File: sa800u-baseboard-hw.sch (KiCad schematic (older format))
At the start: 0 parts

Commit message: removed finished remarks
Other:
- note removed: "GENERAL REMARKS:\n-Nice sheet separation\n-Nice and clear signal labeling\n-Use "kmake get-ignore" inside the repo to make git ignore backup\n files\n-Make folder structure flat - move files ../ \n-Make all the sheets A3 format\n-Avoid "space" in file names use "_" instead"
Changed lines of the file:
@@
 F1 "Level_shift_HDMI.sch" 50
 $EndSheet
-Text Notes 625  6150 0    50   ~ 0
-GENERAL REMARKS:\n-Nice sheet separation\n-Nice and clear signal labeling\n-Use "kmake get-ignore" inside the repo to make git ignore backup\n files\n-Make folder structure flat - move files ../ \n-Make all the sheets A3 format\n-Avoid "space" in file names use "_" instead
 $Sheet
 S 600  7000 500  500

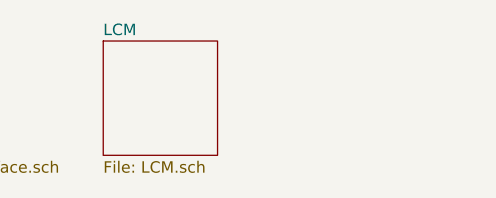
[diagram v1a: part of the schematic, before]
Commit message: finished level shifting circuits for HDMI
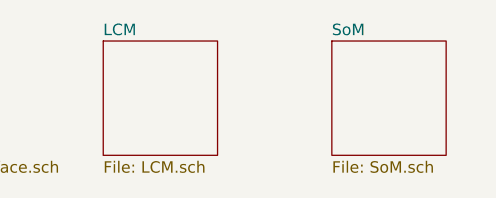
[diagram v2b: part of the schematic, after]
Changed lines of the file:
@@
 $Descr A3 16535 11693
 encoding utf-8
-Sheet 1 7
+Sheet 1 8
 Title ""
 Date ""
@@
 F1 "PoE.sch" 50
 $EndSheet
+$Sheet
+S 7250 7000 500  500
+U 61A4BC4F
+F0 "SoM" 50
+F1 "SoM.sch" 50
+$EndSheet
 $EndSCHEMATC

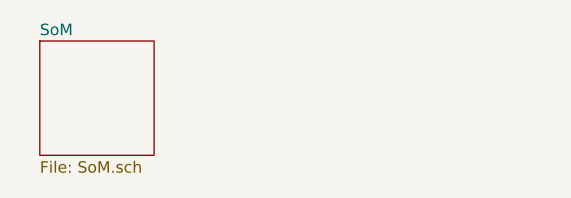
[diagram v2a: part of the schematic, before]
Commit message: added Cameras interface and finished SoM model and symbol
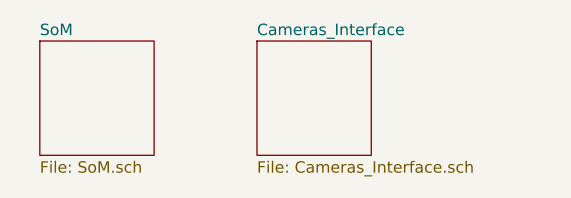
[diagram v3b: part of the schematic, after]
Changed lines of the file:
@@
 $Descr A3 16535 11693
 encoding utf-8
-Sheet 1 8
+Sheet 1 9
 Title ""
 Date ""
@@
 F1 "SoM.sch" 50
 $EndSheet
+$Sheet
+S 8200 7000 500  500
+U 61A60486
+F0 "Cameras_Interface" 50
+F1 "Cameras_Interface.sch" 50
+$EndSheet
 $EndSCHEMATC

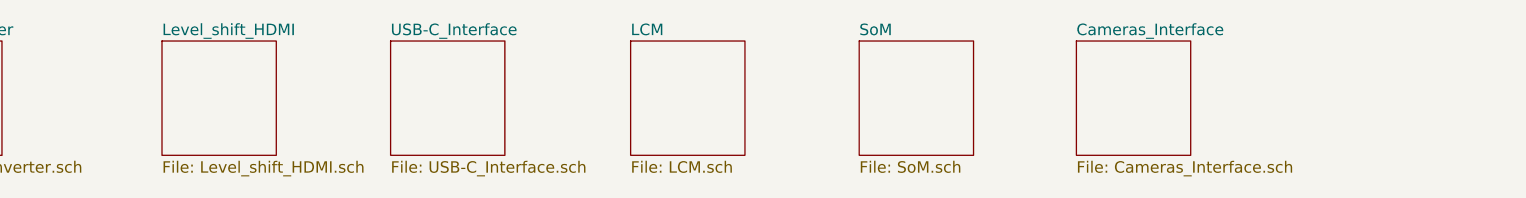
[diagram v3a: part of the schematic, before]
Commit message: work in progress, added usb hub, connectors, and m2 connector
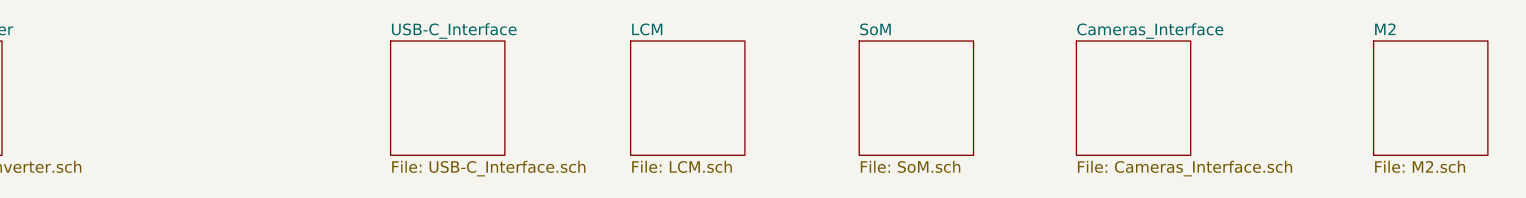
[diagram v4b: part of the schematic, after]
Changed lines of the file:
@@
-$EndSheet
-$Sheet
-S 4200 7000 500  500
-U 61AD1F84
-F0 "Level_shift_HDMI" 50
-F1 "Level_shift_HDMI.sch" 50
 $EndSheet
 $Sheet
@@
 F1 "Cameras_Interface.sch" 50
 $EndSheet
+$Sheet
+S 9500 7000 500  500
+U 61B13669
+F0 "M2" 50
+F1 "M2.sch" 50
+$EndSheet
 $EndSCHEMATC

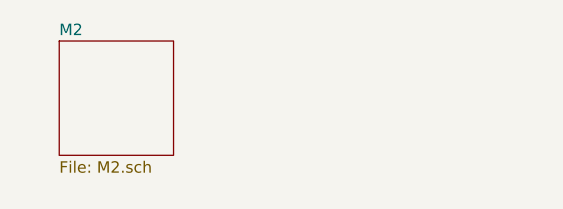
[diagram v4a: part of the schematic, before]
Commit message: added sd card, buttons, rtc battery - work in progress
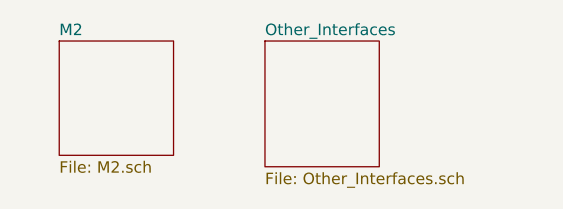
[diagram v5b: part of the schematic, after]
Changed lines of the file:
@@
 $Descr A3 16535 11693
 encoding utf-8
-Sheet 1 9
+Sheet 1 10
 Title ""
 Date ""
@@
 F1 "M2.sch" 50
 $EndSheet
+$Sheet
+S 10400 7000 500  550
+U 61C01D88
+F0 "Other_Interfaces" 50
+F1 "Other_Interfaces.sch" 50
+$EndSheet
 $EndSCHEMATC

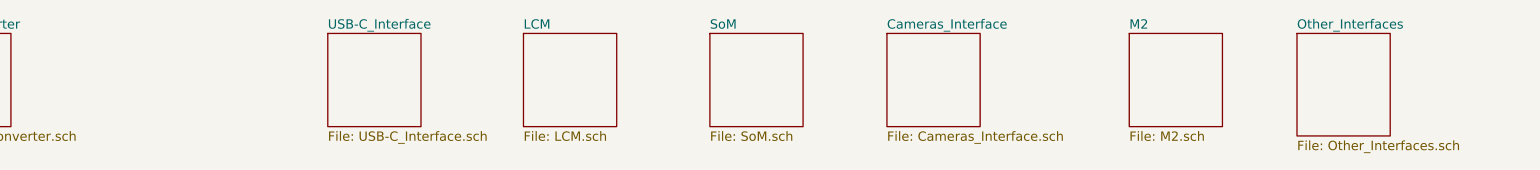
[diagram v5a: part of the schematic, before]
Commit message: added components to pcb and fixed corresponding errors
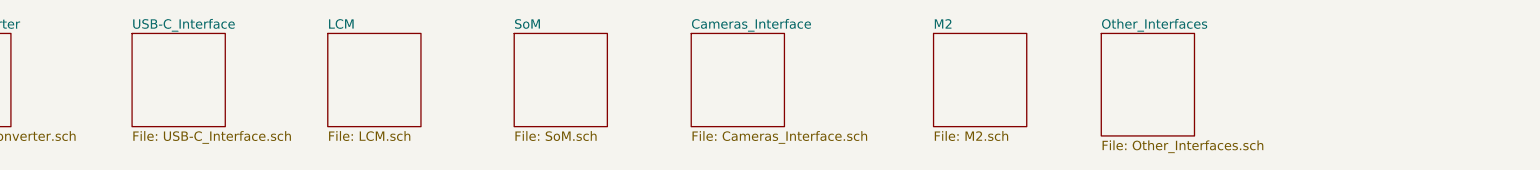
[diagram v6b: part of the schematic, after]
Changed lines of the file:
@@
 $EndSheet
 $Sheet
-S 5200 7000 500  500
+S 4150 7000 500  500
 U 61A2F307
 F0 "USB-C_Interface " 50
@@
 $EndSheet
 $Sheet
-S 6250 7000 500  500
+S 5200 7000 500  500
 U 61BD2CC1
 F0 "LCM" 50
@@
 $EndSheet
 $Sheet
-S 7250 7000 500  500
+S 6200 7000 500  500
 U 61A4BC4F
 F0 "SoM" 50
@@
 $EndSheet
 $Sheet
-S 8200 7000 500  500
+S 7150 7000 500  500
 U 61A60486
 F0 "Cameras_Interface" 50
@@
 $EndSheet
 $Sheet
-S 9500 7000 500  500
+S 8450 7000 500  500
 U 61B13669
 F0 "M2" 50
@@
 $EndSheet
 $Sheet
-S 10400 7000 500  550
+S 9350 7000 500  550
 U 61C01D88
 F0 "Other_Interfaces" 50

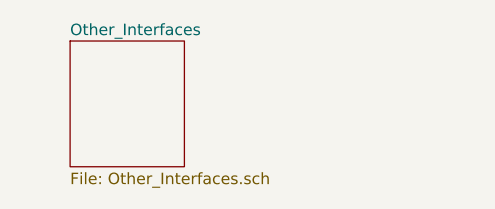
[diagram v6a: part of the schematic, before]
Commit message: added first version of board layout
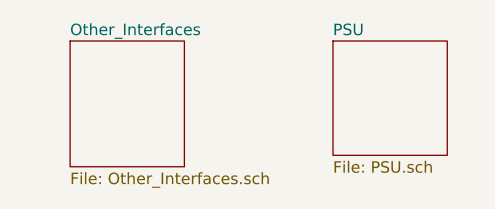
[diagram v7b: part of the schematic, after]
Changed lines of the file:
@@
 $Descr A3 16535 11693
 encoding utf-8
-Sheet 1 10
+Sheet 1 11
 Title ""
 Date ""
@@
 F1 "Other_Interfaces.sch" 50
 $EndSheet
+$Sheet
+S 10500 7000 500  500
+U 61B0DC30
+F0 "PSU" 50
+F1 "PSU.sch" 50
+$EndSheet
 $EndSCHEMATC

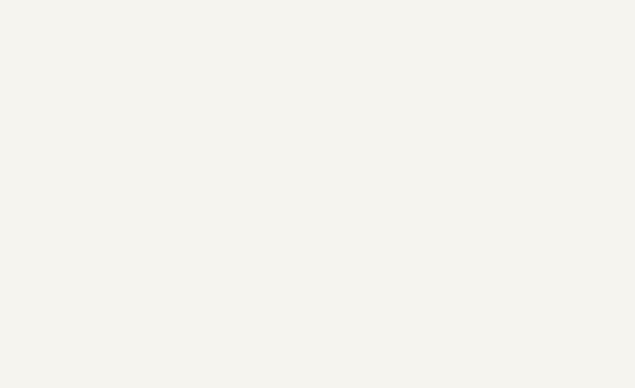
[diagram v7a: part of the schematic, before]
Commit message: permanently added mounting holes
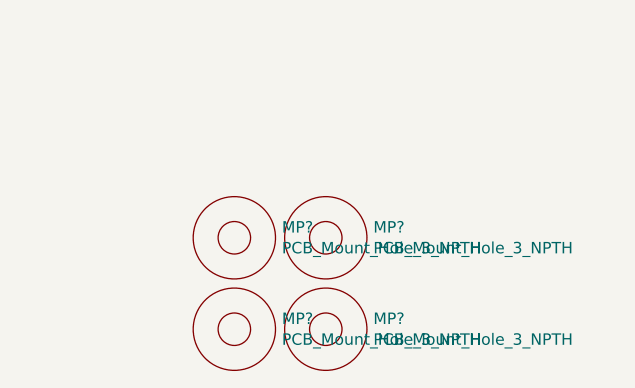
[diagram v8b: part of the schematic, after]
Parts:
- added MP? (x4): PCB_Mount_Hole_3_NPTH, antmicro-footprints:mounting-hole-3mm-NPTH, symbol antmicroMechanicalParts:PCB_Mount_Hole_3_NPTH
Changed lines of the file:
@@
 F1 "PSU.sch" 50
 $EndSheet
+$Comp
+L antmicroMechanicalParts:PCB_Mount_Hole_3_NPTH MP?
+U 1 1 61B52107
+P 12050 8050
+F 0 "MP?" H 12258 8096 50  0000 L CNN
+F 1 "PCB_Mount_Hole_3_NPTH" H 12258 8005 50  0000 L CNN
+F 2 "antmicro-footprints:mounting-hole-3mm-NPTH" H 12850 8750 50  0001 C CNN
+F 3 "" H 13000 8850 50  0001 C CNN
+	1    12050 8050
+	1    0    0    -1
+$EndComp
+$Comp
+L antmicroMechanicalParts:PCB_Mount_Hole_3_NPTH MP?
+U 1 1 61B52579
+P 12450 8050
+F 0 "MP?" H 12658 8096 50  0000 L CNN
+F 1 "PCB_Mount_Hole_3_NPTH" H 12658 8005 50  0000 L CNN
+F 2 "antmicro-footprints:mounting-hole-3mm-NPTH" H 13250 8750 50  0001 C CNN
+F 3 "" H 13400 8850 50  0001 C CNN
+	1    12450 8050
+	1    0    0    -1
+$EndComp
+$Comp
+L antmicroMechanicalParts:PCB_Mount_Hole_3_NPTH MP?
+U 1 1 61B52868
+P 12050 8450
+F 0 "MP?" H 12258 8496 50  0000 L CNN
+F 1 "PCB_Mount_Hole_3_NPTH" H 12258 8405 50  0000 L CNN
+F 2 "antmicro-footprints:mounting-hole-3mm-NPTH" H 12850 9150 50  0001 C CNN
+F 3 "" H 13000 9250 50  0001 C CNN
+	1    12050 8450
+	1    0    0    -1
+$EndComp
+$Comp
+L antmicroMechanicalParts:PCB_Mount_Hole_3_NPTH MP?
+U 1 1 61B52B11
+P 12450 8450
+F 0 "MP?" H 12658 8496 50  0000 L CNN
+F 1 "PCB_Mount_Hole_3_NPTH" H 12658 8405 50  0000 L CNN
+F 2 "antmicro-footprints:mounting-hole-3mm-NPTH" H 13250 9150 50  0001 C CNN
+F 3 "" H 13400 9250 50  0001 C CNN
+	1    12450 8450
+	1    0    0    -1
+$EndComp
 $EndSCHEMATC
